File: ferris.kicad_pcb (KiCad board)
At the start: 2 copper layers, 225 x 95.2 mm, 98 parts, among them J1 USB C, K0_0 KEYSW, K0_1 KEYSW, K0_2 KEYSW, K0_3 KEYSW, K0_4 KEYSW, K0_5 KEYSW, K0_6 KEYSW, K0_7 KEYSW, K0_8 KEYSW, K0_9 KEYSW, K1_0 KEYSW, K1_1 KEYSW, K1_2 KEYSW, K1_3 KEYSW, K1_4 KEYSW, K1_5 KEYSW, K1_6 KEYSW, K1_7 KEYSW, K1_8 KEYSW, K1_9 KEYSW, K2_0 KEYSW, K2_1 KEYSW, K2_2 KEYSW, K2_3 KEYSW, K2_4 KEYSW, K2_5 KEYSW, K2_6 KEYSW, K2_7 KEYSW, K2_8 KEYSW, K2_9 KEYSW, K3_3 KEYSW, K3_4 KEYSW, K3_5 KEYSW, K3_6 KEYSW, SW1 SW_PUSH, U1 ATmega32U4-AU, U2 MCP23017_SO, Y1 Crystal

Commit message: Added LED on LHS
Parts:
- added D1: WS2812B, LED_SMD:LED_WS2812B_PLCC4_5.0x5.0mm_P3.2mm, F.Cu at (112.6, 69.7)
- added U3: TCA9535RTWR, Package_DFN_QFN:WQFN-24-1EP_4x4mm_P0.5mm_EP2.45x2.45mm, B.Cu at (207.8, 82.4)
- moved R6 3.91 mm to (117.9, 68.3), turned to 270 degrees
- moved R5 1.14 mm to (120.6, 68.3), turned to 270 degrees
- moved F1 0.57 mm to (119.3, 71.5)
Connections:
- J1 pad A8: (no net) -> Net-(J1-PadA8)
- J1 pad B8: (no net) -> Net-(J1-PadB8)
- U1 pad 1: (no net) -> Net-(U1-Pad1)
- U1 pad 12: (no net) -> Net-(U1-Pad12)
- U1 pad 20: (no net) -> Net-(U1-Pad20)
- U1 pad 21: (no net) -> Net-(U1-Pad21)
- U1 pad 22: (no net) -> Net-(U1-Pad22)
- U1 pad 25: (no net) -> Net-(U1-Pad25)
- U1 pad 31: (no net) -> Net-(U1-Pad31)
- U1 pad 32: (no net) -> Net-(U1-Pad32)
- U1 pad 36: (no net) -> Net-(U1-Pad36)
- U1 pad 37: (no net) -> Net-(U1-Pad37)
- U1 pad 38: (no net) -> Net-(U1-Pad38)
- U1 pad 39: (no net) -> Net-(U1-Pad39)
- U1 pad 40: (no net) -> Net-(D1-Pad4)
- U1 pad 42: (no net) -> Net-(U1-Pad42)
- U1 pad 8: (no net) -> Net-(U1-Pad8)
- U2 pad 11: (no net) -> Net-(U2-Pad11)
- U2 pad 14: (no net) -> Net-(U2-Pad14)
- U2 pad 19: (no net) -> Net-(U2-Pad19)
- U2 pad 20: (no net) -> Net-(U2-Pad20)
- U2 pad 26: (no net) -> Net-(U2-Pad26)
- U2 pad 27: (no net) -> Net-(U2-Pad27)
- U2 pad 28: (no net) -> Net-(U2-Pad28)
- U2 pad 5: (no net) -> Net-(U2-Pad5)
- U2 pad 6: (no net) -> Net-(U2-Pad6)
- U2 pad 7: (no net) -> Net-(U2-Pad7)
- U2 pad 8: (no net) -> Net-(U2-Pad8)
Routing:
- net Net-(D1-Pad4): track 0.00 -> 44.9 mm, vias 0 -> 2
- net VCC: track 14.4 -> 26.0 mm, vias 0 -> 2
- net GND: track 223.9 -> 234.8 mm, vias 4 -> 5
- net +5V: track 183.6 -> 191.1 mm
- net Net-(J1-PadB5): track 4.29 -> 10.7 mm
- net Net-(J1-PadA6): track 16.7 -> 12.2 mm, vias 0 -> 2
- net Net-(J1-PadA5): track 3.36 -> 6.34 mm
- net Net-(J1-PadA7): track 12.7 -> 14.8 mm, vias 0 -> 2

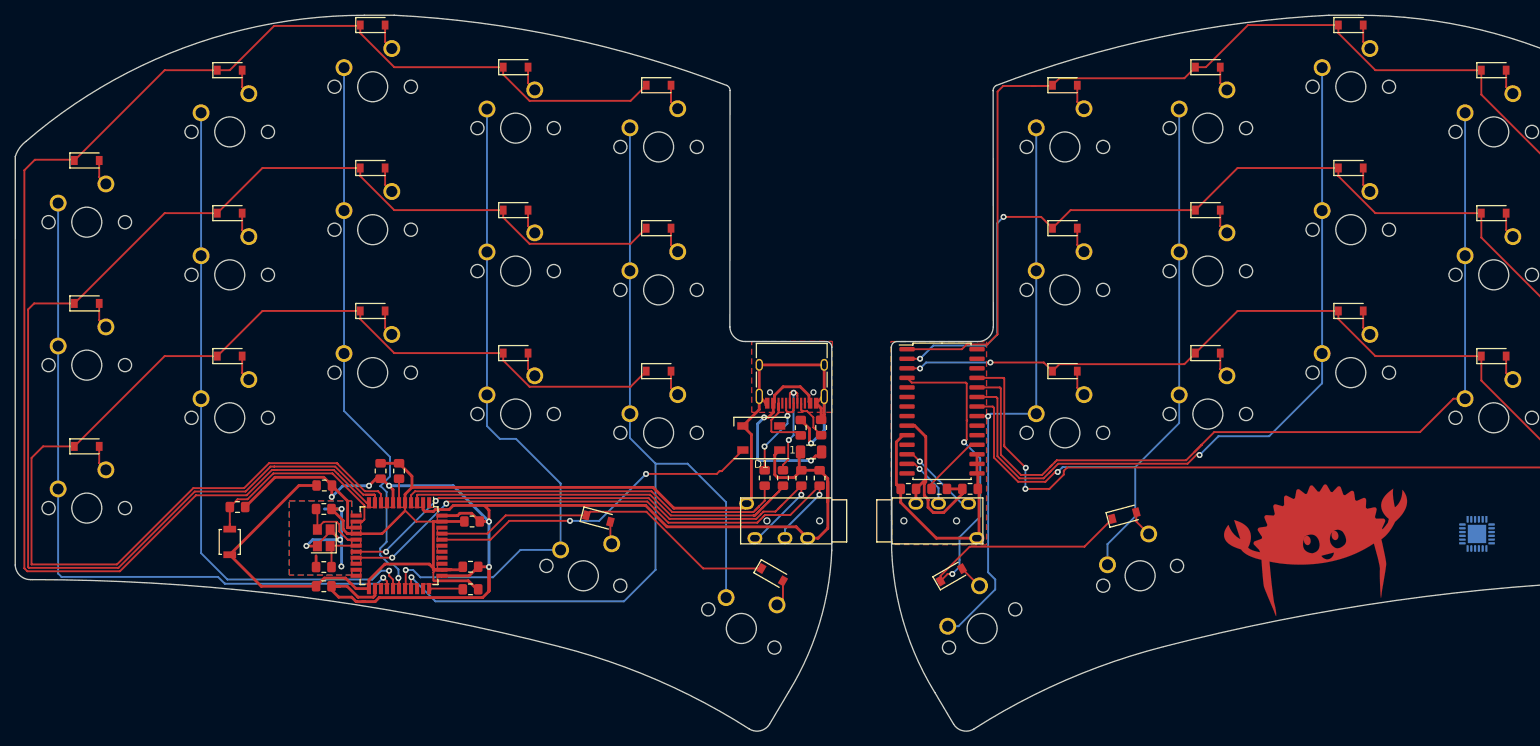
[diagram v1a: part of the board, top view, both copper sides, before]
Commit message: Moved I2C resistors to RHS, moved LED
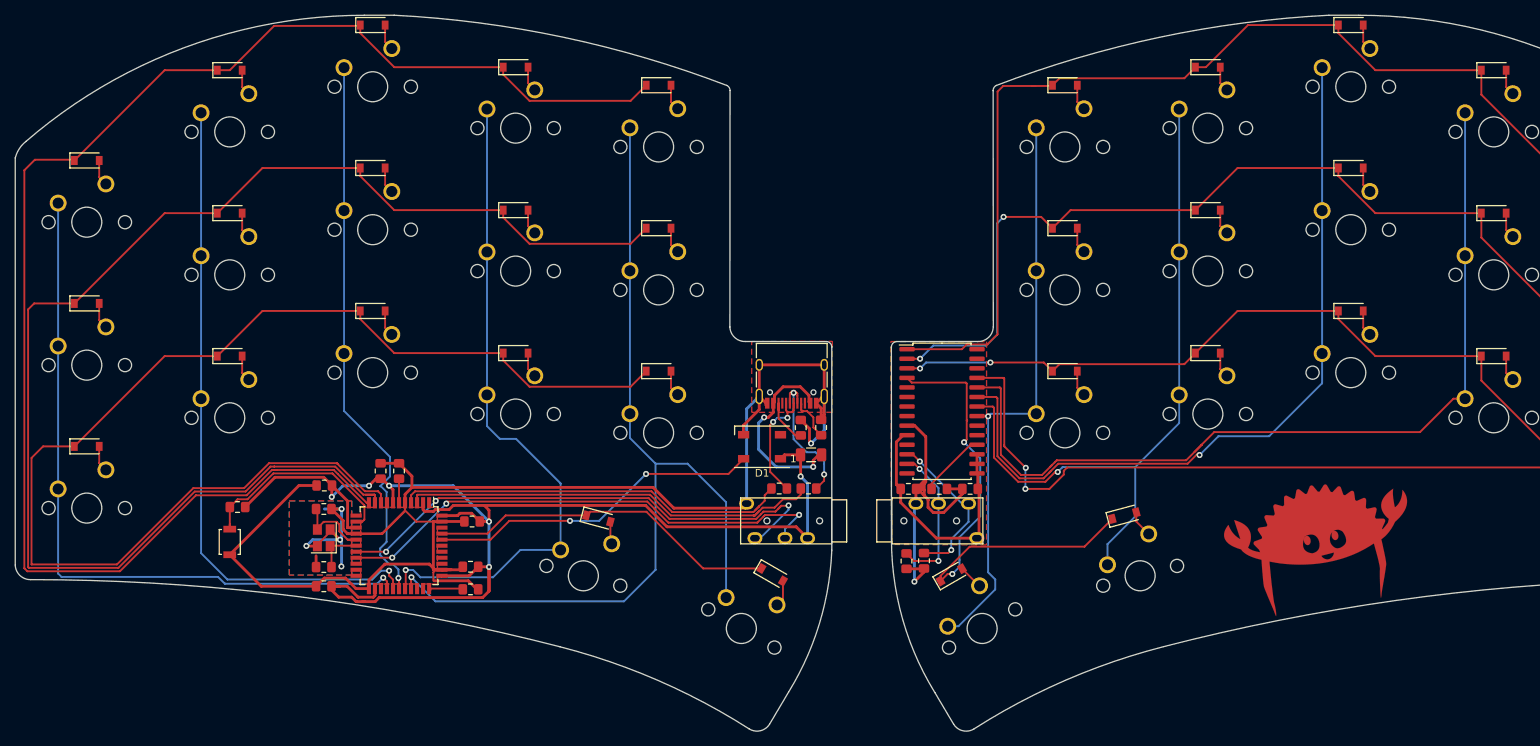
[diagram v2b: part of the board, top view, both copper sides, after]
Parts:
- removed U3: TCA9535RTWR, Package_DFN_QFN:WQFN-24-1EP_4x4mm_P0.5mm_EP2.45x2.45mm
- moved R7 17.8 mm to (131.9, 86.0), turned to 270 degrees
- moved R8 17.7 mm to (134.3, 86.0)
- moved R3 3.67 mm to (118.9, 76.4), turned to 0 degrees
- moved R4 2.38 mm to (115.0, 76.4), turned to 0 degrees
- moved D1 1.17 mm to (112.8, 70.8)
- moved F1 0.39 mm to (119.3, 71.9)
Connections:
- R7 pad 1: Net-(Jack0-PadT) -> Net-(Jack1-PadR1)
- R7 pad 2: +5V -> VDD
- R8 pad 1: +5V -> Net-(Jack1-PadT)
- R8 pad 2: Net-(Jack0-PadR1) -> VDD
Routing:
- net VDD: track 25.2 -> 44.6 mm, vias 0 -> 1
- net +5V: track 191.1 -> 178.2 mm, vias 5 -> 6
- net Net-(Jack1-PadR1): track 7.59 -> 19.9 mm, vias 1 -> 2
- net Net-(Jack1-PadT): track 10.9 -> 21.8 mm, vias 1 -> 2
- net Net-(Jack0-PadR1): track 77.0 -> 67.8 mm
- net Net-(Jack0-PadT): track 75.6 -> 70.1 mm
- net GND: track 234.8 -> 239.9 mm
- net Net-(J1-PadA7): track 14.8 -> 19.5 mm
- net Net-(J1-PadA6): track 12.2 -> 16.0 mm
- net /D-: track 58.1 -> 56.1 mm
- net Net-(J1-PadB5): track 10.7 -> 8.94 mm
- net VCC: track 26.0 -> 27.0 mm
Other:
- outline, holes or cut-outs redrawn

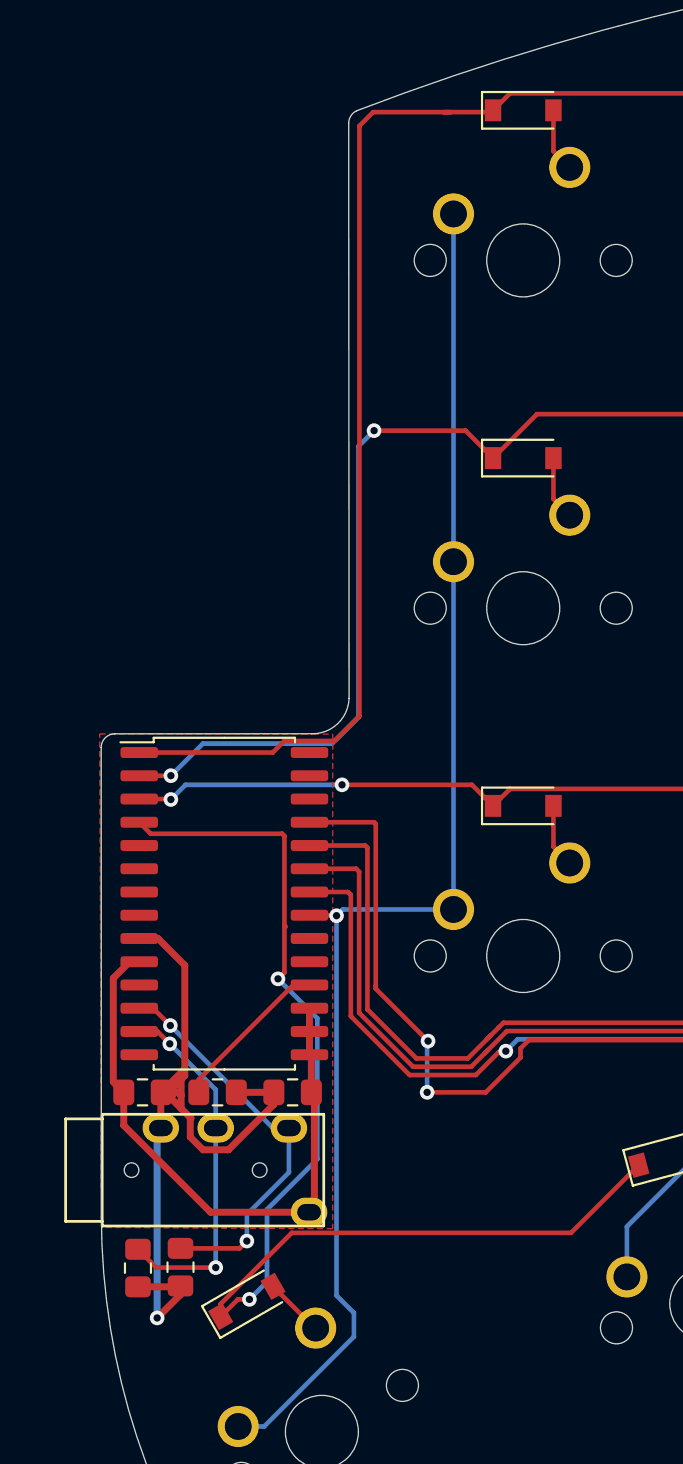
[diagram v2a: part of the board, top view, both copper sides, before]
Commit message: Replaced MCP23017 with PCA9539PW
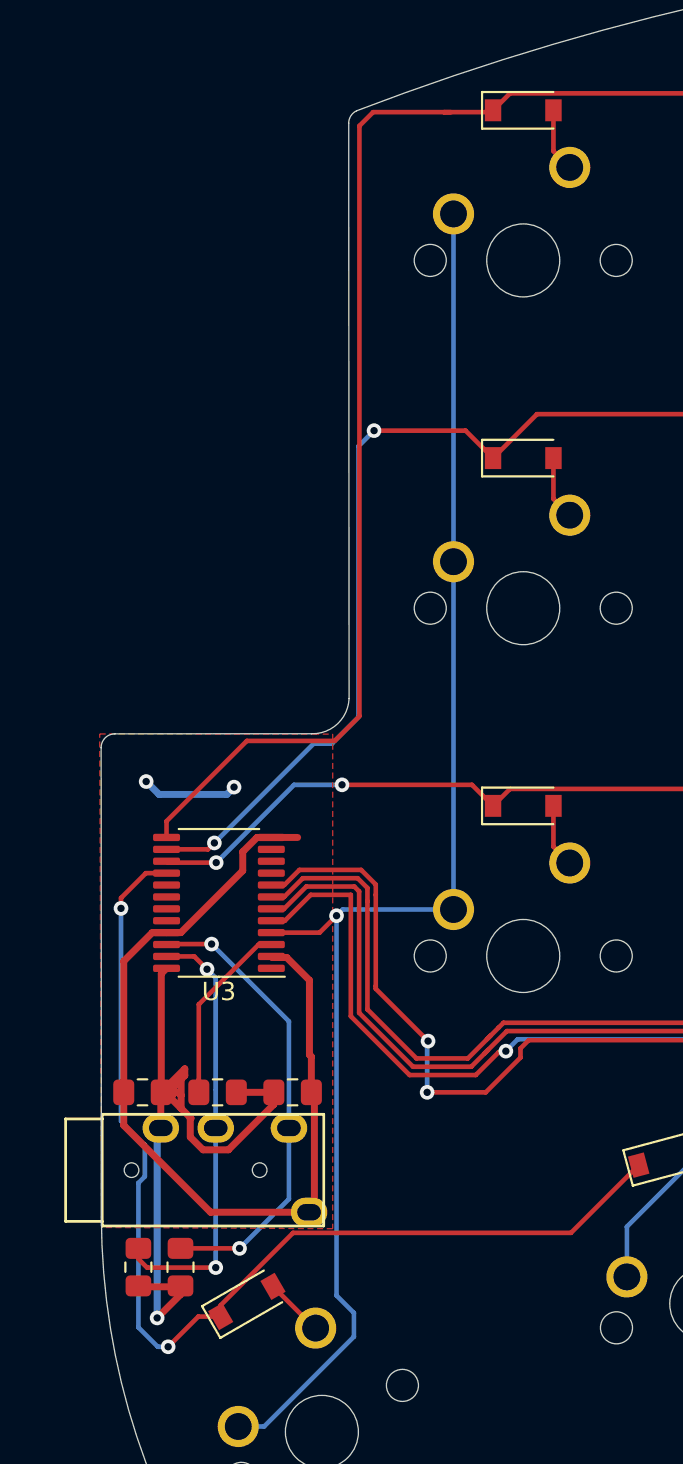
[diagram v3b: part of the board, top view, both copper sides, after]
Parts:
- removed U2: MCP23017_SO, Package_SO:SOIC-28W_7.5x17.9mm_P1.27mm
- added U3: PCA9539PW, Package_SO:TSSOP-24_4.4x7.8mm_P0.65mm, F.Cu at (136.4, 66.1)
- moved R7 2.33 mm to (134.3, 86.0)
- moved R8 2.30 mm to (132.0, 86.0)
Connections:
- R7 pad 1: Net-(Jack1-PadR1) -> Net-(Jack1-PadT)
- R8 pad 1: Net-(Jack1-PadT) -> Net-(Jack1-PadR1)
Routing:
- net VSS: track 33.5 -> 54.8 mm, vias 0 -> 2
- net /row1,3: track 64.9 -> 59.4 mm
- net Net-(Jack1-PadT): track 21.8 -> 26.1 mm
- net Net-(Jack1-PadR1): track 19.9 -> 24.0 mm
- net /col6: track 94.4 -> 97.0 mm
- net /col5: track 77.8 -> 80.3 mm
- net Net-(R9-Pad1): track 8.88 -> 10.8 mm
- net VDD: track 44.6 -> 42.7 mm
- net /col7: track 102.5 -> 104.0 mm
- net /row1,0: track 142.4 -> 143.4 mm
- net /col9: track 137.6 -> 137.0 mm

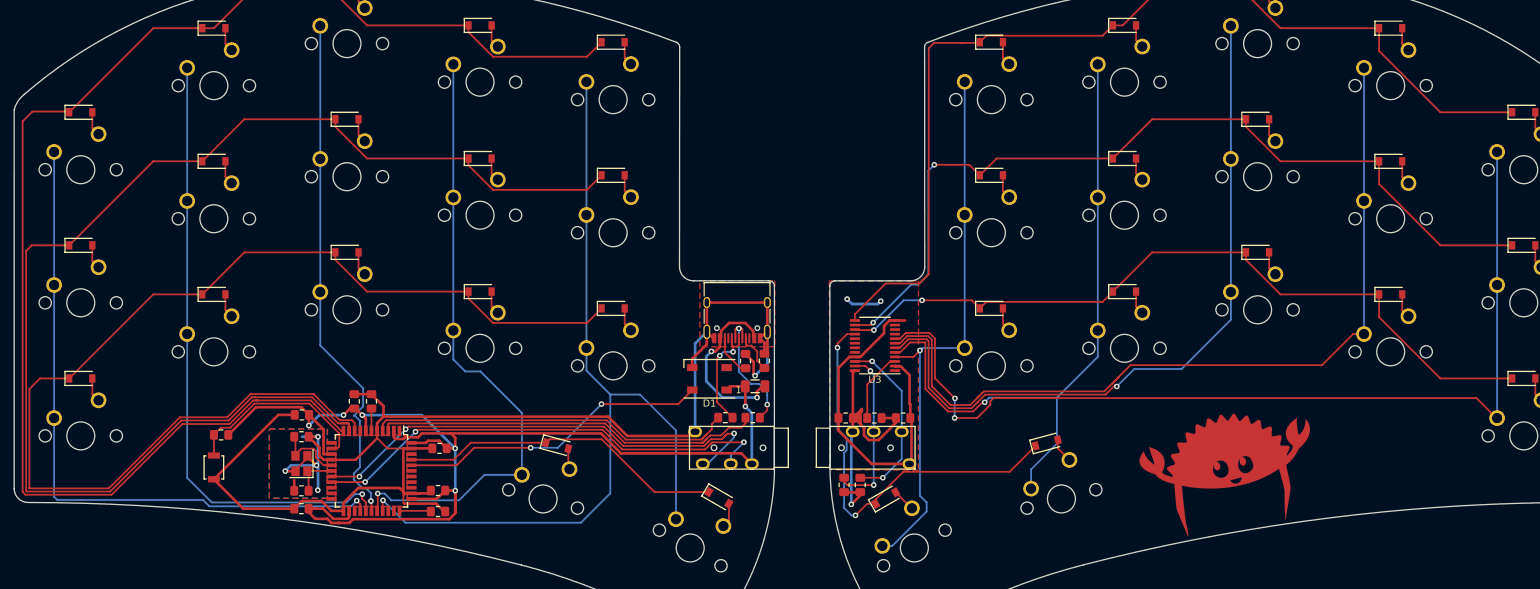
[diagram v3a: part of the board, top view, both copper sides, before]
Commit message: Repositioned the components near the inner edges
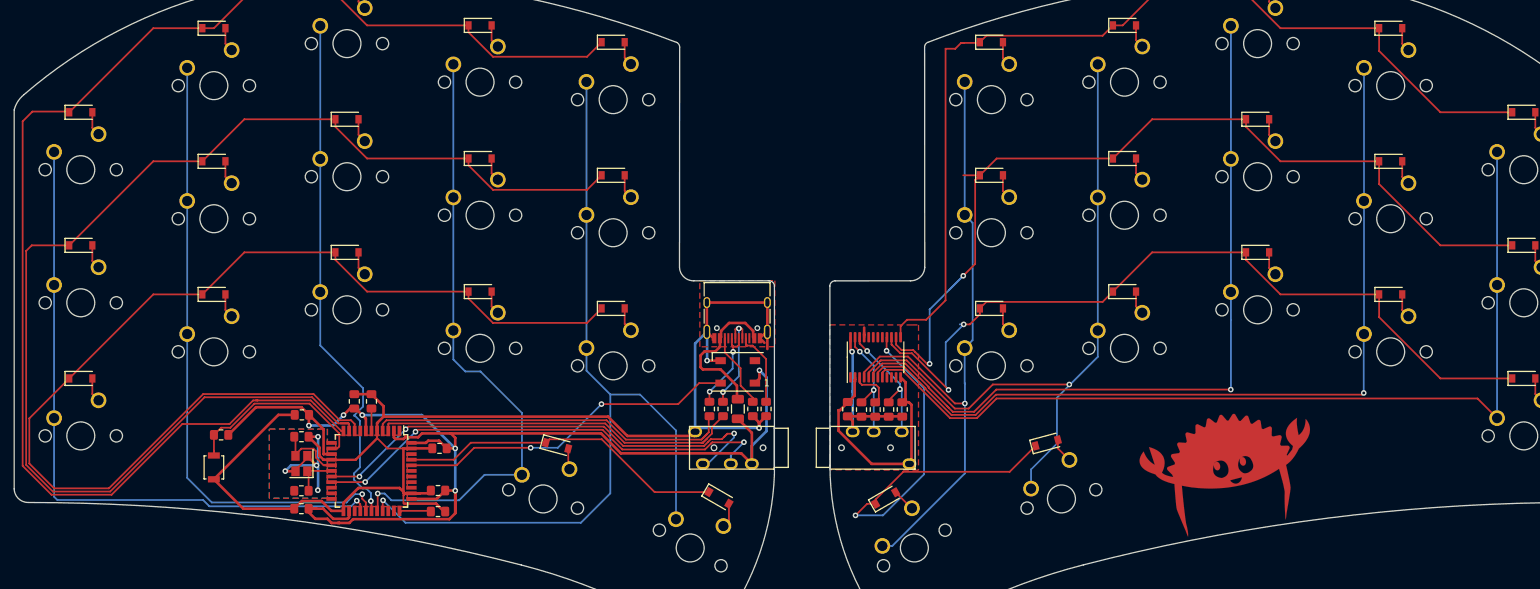
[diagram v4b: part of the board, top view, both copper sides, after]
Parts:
- moved R7 11.5 mm to (138.3, 75.2)
- moved R8 11.0 mm to (134.5, 75.2)
- moved R6 6.92 mm to (118.9, 75.2), turned to 90 degrees
- moved R5 6.87 mm to (120.8, 75.2), turned to 90 degrees
- moved R3 4.42 mm to (114.7, 75.2), turned to 90 degrees
- moved D1 4.16 mm to (116.8, 69.9)
- moved F1 4.07 mm to (116.8, 75.2), turned to 90 degrees
- moved R4 2.59 mm to (112.8, 75.2), turned to 90 degrees
- moved U3 1.68 mm to (136.5, 67.8), turned to 90 degrees
- moved C10 1.30 mm to (132.5, 75.2), turned to 270 degrees
- moved C9 1.23 mm to (140.3, 75.2), turned to 270 degrees
- moved R9 1.22 mm to (136.4, 75.2), turned to 270 degrees
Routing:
- net VDD: track 42.7 -> 24.1 mm
- net VSS: track 54.8 -> 36.3 mm, vias 2 -> 0
- net /col5: track 80.3 -> 91.7 mm
- net +5V: track 178.2 -> 187.8 mm
- net Net-(Jack1-PadR1): track 24.0 -> 17.1 mm
- net Net-(Jack1-PadT): track 26.1 -> 19.4 mm
- net /row1,2: track 109.7 -> 116.1 mm
- net /row1,1: track 125.9 -> 131.3 mm
- net /col9: track 137.0 -> 131.8 mm, vias 2 -> 0
- net /col7: track 104.0 -> 108.9 mm
- net /row1,3: track 59.4 -> 64.2 mm
- net Net-(J1-PadA5): track 6.34 -> 11.1 mm
- net Net-(R9-Pad1): track 10.8 -> 6.09 mm
- net /row0,2: track 165.1 -> 160.5 mm
- net Net-(D1-Pad4): track 44.6 -> 49.0 mm
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
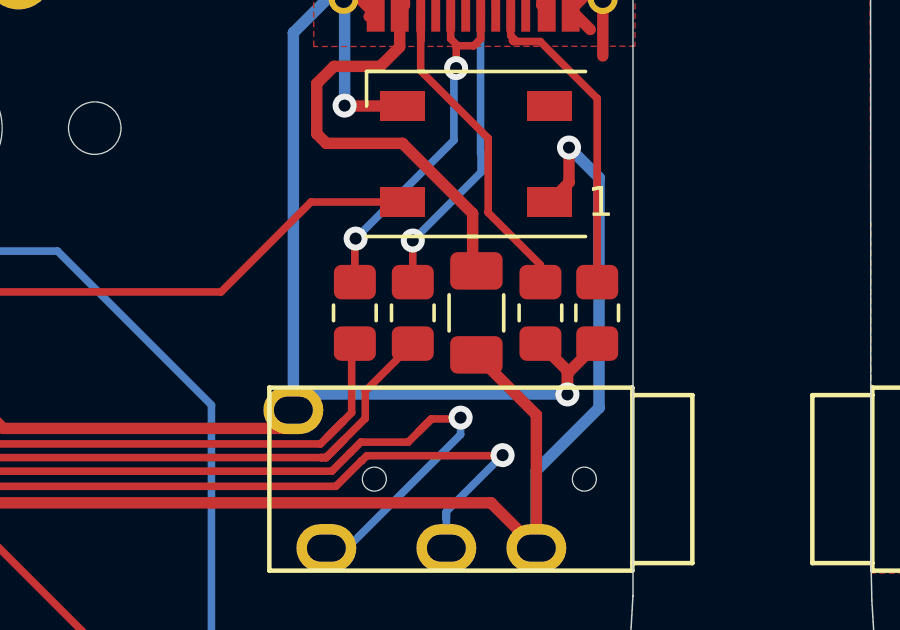
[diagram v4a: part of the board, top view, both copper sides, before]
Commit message: Fixed a minor DRC error
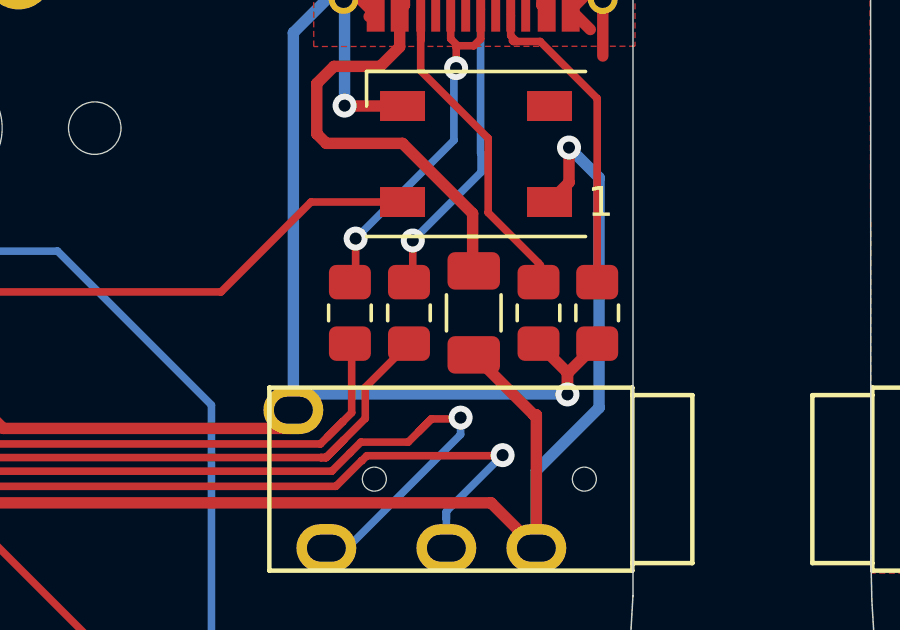
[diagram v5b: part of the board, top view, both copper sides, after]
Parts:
- moved R4 0.17 mm to (112.6, 75.2)
- moved R3 0.13 mm to (114.6, 75.2)
- moved F1 0.09 mm to (116.7, 75.2)
- moved R6 0.06 mm to (118.9, 75.2)
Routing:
- net Net-(J1-PadB5): track 12.6 -> 13.2 mm

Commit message: Cleaned up some tracks. Final stuff editing now
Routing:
- net VSS: track 36.3 -> 49.2 mm
- net /row1,1: track 131.3 -> 123.4 mm
- net /col6: track 99.0 -> 103.5 mm
- net /col0: track 95.0 -> 91.3 mm
- net /col7: track 108.9 -> 105.6 mm
- net GND: track 236.5 -> 233.5 mm
- net /row1,0: track 140.4 -> 138.7 mm
- net /col2: track 74.4 -> 73.3 mm
- net /row1,3: track 64.2 -> 65.1 mm
- net Net-(Jack1-PadT): track 19.4 -> 18.8 mm
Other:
- board text added: "“Getting an education was a bit like a communicable sexual disease. It made you unsuitable for a lot of jobs, and then you had the urge to pass it on.”"

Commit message: Rotated pinky col
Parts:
- removed the G*** at (191.8, 59.5)
- removed the G*** at (62.5, 60.0)
- moved C4 40.9 mm to (84.3, 108.4)
- moved C5 40.9 mm to (76.8, 110.3)
- moved R1 40.9 mm to (65.3, 113.2)
- moved R9 40.9 mm to (158.6, 109.5)
- moved C10 40.9 mm to (154.7, 109.5)
- moved C3 40.9 mm to (76.7, 123.7)
- moved C6 40.9 mm to (96.2, 121.1)
- moved C7 40.9 mm to (96.4, 115.1)
- moved C8 40.9 mm to (86.7, 108.4)
- moved C9 40.9 mm to (162.5, 109.5)
- moved D0_1 40.9 mm to (64.2, 55.1)
- moved D0_2 40.9 mm to (83.2, 49.1)
- moved D0_3 40.9 mm to (102.2, 54.7)
- moved D0_4 40.9 mm to (121.2, 57.1)
- moved D0_5 40.9 mm to (175.2, 57.1)
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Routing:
- net /row1,0: track 138.7 -> 146.9 mm
- net /row1,1: track 123.4 -> 129.8 mm
- net /col0: track 91.3 -> 94.9 mm
- net /row0,1: track 183.8 -> 181.0 mm
- net /row0,0: track 201.3 -> 198.6 mm
- net /row0,2: track 160.5 -> 158.1 mm
- net /col9: track 131.8 -> 133.9 mm
- net Net-(Jack1-PadT): track 18.8 -> 19.4 mm
- net VDD: track 24.1 -> 24.7 mm
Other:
- board size 225 x 95.2 mm -> 237.4 x 95.2 mm
- board text removed: "“Getting an education was a bit like a communicable sexual disease. It made you unsuitable for a lot of jobs, and then you had the urge to pass it on.”"
